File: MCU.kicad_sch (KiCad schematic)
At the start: 55 parts, among them IC1 BALFHB-WL-02D3, J2 Conn_Coaxial, J3 Led, Q2 S8050, Q3 S8050, SW1 SW_Push, U4 BGS12WN6E6327, U5 STM32WLE5CCUx, X1 NX2016SA-32MHZ, Y1 NX2012SA 32.768KHz

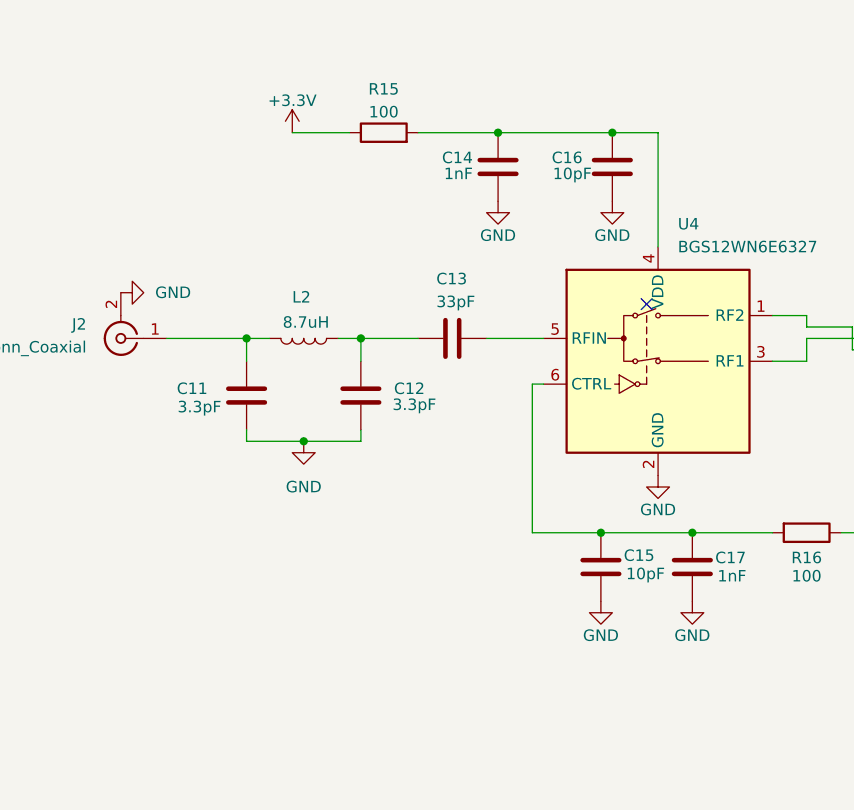
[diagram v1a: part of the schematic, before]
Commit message: removed polarity protection and fixed component placement
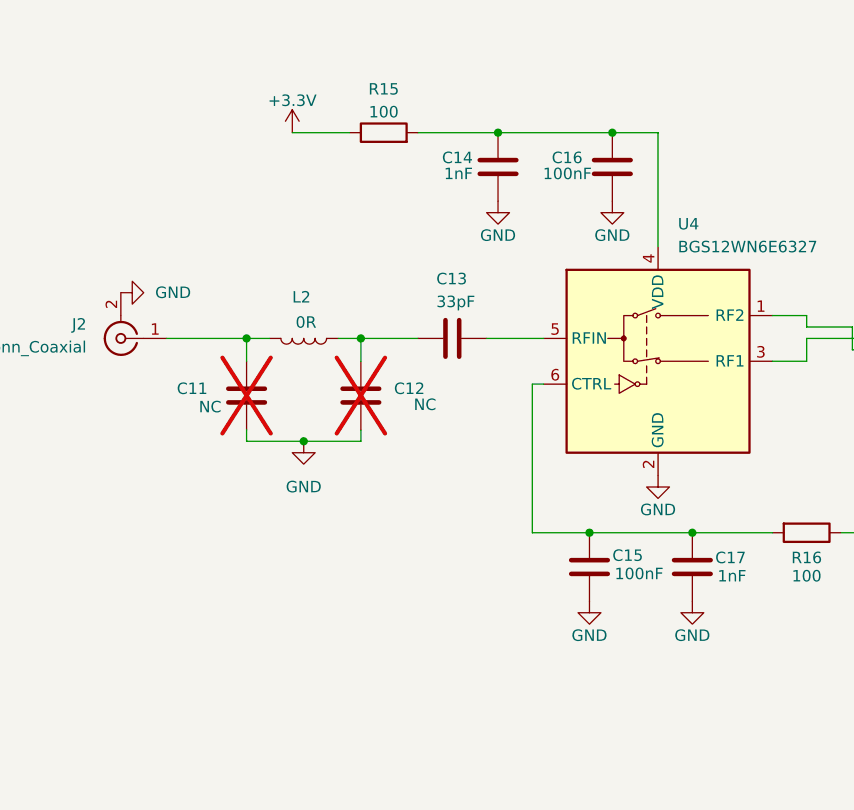
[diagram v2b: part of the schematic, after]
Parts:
- C11, C12: value 3.3pF -> NC; now not fitted; now left out of the parts list
- C15, C16: value 10pF -> 100nF
- L2: value 8.7uH -> 0R
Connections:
- no-connect marks 19 -> 18
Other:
- moved on the sheet: C15
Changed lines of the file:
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@@
 	)
 	(junction
+		(at 99.06 186.69)
+		(diameter 0)
+		(color 0 0 0 0)
+	)
+	(junction
 		(at 200.66 200.66)
 		(diameter 0)
@@
 	)
 	(junction
-		(at 100.33 186.69)
-		(diameter 0)
-		(color 0 0 0 0)
-	)
-	(junction
 		(at 273.05 40.64)
 		(diameter 0)
@@
 	)
 	(no_connect
-		(at 105.41 161.29)
-	)
-	(no_connect
 		(at 278.13 162.56)
 	)
@@
 	(wire
 		(pts
+			(xy 99.06 186.69) (xy 110.49 186.69)
+		)
+		(stroke
+			(width 0)
+			(type default)
+		)
+	)
+	(wire
+		(pts
 			(xy 119.38 167.64) (xy 123.19 167.64)
 		)
@@
 	(wire
 		(pts
+			(xy 99.06 186.69) (xy 92.71 186.69)
+		)
+		(stroke
+			(width 0)
+			(type default)
+		)
+	)
+	(wire
+		(pts
 			(xy 219.71 153.67) (xy 219.71 151.13)
 		)
@@
 	(wire
 		(pts
-			(xy 100.33 186.69) (xy 92.71 186.69)
-		)
-		(stroke
-			(width 0)
-			(type default)
-		)
-	)
-	(wire
-		(pts
 			(xy 144.78 165.1) (xy 147.32 165.1)
 		)
@@
 	(wire
 		(pts
-			(xy 110.49 186.69) (xy 100.33 186.69)
-		)
-		(stroke
-			(width 0)
-			(type default)
-		)
-	)
-	(wire
-		(pts
 			(xy 247.65 129.54) (xy 247.65 132.08)
 		)
@@
 	(symbol
 		(lib_id "Device:C")
-		(at 100.33 190.5 0)
+		(at 99.06 190.5 0)
 		(unit 1)
 		(exclude_from_sim no)
@@
 		(dnp no)
 		(property "Reference" "C15"
-			(at 102.87 189.23 0)
+			(at 101.6 189.23 0)
 			(effects
 				(font
@@
 			)
 		)
-		(property "Value" "10pF"
-			(at 103.124 191.262 0)
+		(property "Value" "100nF"
+			(at 101.854 191.262 0)
 			(effects
 				(font
@@
 		)
 		(property "Footprint" "Capacitor_SMD:C_0402_1005Metric_Pad0.74x0.62mm_HandSolder"
-			(at 101.2952 194.31 0)
+			(at 100.0252 194.31 0)
 			(effects
 				(font
@@
 		)
 		(property "Datasheet" "~"
-			(at 100.33 190.5 0)
+			(at 99.06 190.5 0)
 			(effects
 				(font
@@
 		)
 		(property "Description" ""
-			(at 100.33 190.5 0)
+			(at 99.06 190.5 0)
 			(effects
 				(font
@@
 		)
 		(property "MANUFACTURER" ""
-			(at 100.33 190.5 0)
+			(at 99.06 190.5 0)
 			(effects
 				(font
@@
 		)
 		(property "MAXIMUM_PACKAGE_HEIGHT" ""
-			(at 100.33 190.5 0)
+			(at 99.06 190.5 0)
 			(effects
 				(font
@@
 		)
 		(property "PARTREV" ""
-			(at 100.33 190.5 0)
+			(at 99.06 190.5 0)
 			(effects
 				(font
@@
 		)
 		(property "STANDARD" ""
-			(at 100.33 190.5 0)
+			(at 99.06 190.5 0)
 			(effects
 				(font
@@
 		(unit 1)
 		(exclude_from_sim no)
-		(in_bom yes)
+		(in_bom no)
 		(on_board yes)
-		(dnp no)
+		(dnp yes)
 		(property "Reference" "C12"
 			(at 80.772 170.688 0)
@@
 			)
 		)
-		(property "Value" "3.3pF"
+		(property "Value" "NC"
 			(at 82.042 172.466 0)
 			(effects
@@
 			)
 		)
-		(property "Value" "8.7uH"
+		(property "Value" "0R"
 			(at 67.564 163.322 90)
 			(effects
@@
 	(symbol
 		(lib_id "power:GND")
-		(at 100.33 194.31 0)
+		(at 99.06 194.31 0)
 		(unit 1)
 		(exclude_from_sim no)
@@
 		(dnp no)
 		(property "Reference" "#PWR016"
-			(at 100.33 200.66 0)
+			(at 99.06 200.66 0)
 			(effects
 				(font
@@
 		)
 		(property "Value" "GND"
-			(at 100.33 198.12 0)
+			(at 99.06 198.12 0)
 			(effects
 				(font
@@
 		)
 		(property "Footprint" ""
-			(at 100.33 194.31 0)
+			(at 99.06 194.31 0)
 			(effects
 				(font
@@
 		)
 		(property "Datasheet" ""
-			(at 100.33 194.31 0)
+			(at 99.06 194.31 0)
 			(effects
 				(font
@@
 		)
 		(property "Description" ""
-			(at 100.33 194.31 0)
+			(at 99.06 194.31 0)
 			(effects
 				(font
@@
 		(unit 1)
 		(exclude_from_sim no)
-		(in_bom yes)
+		(in_bom no)
 		(on_board yes)
-		(dnp no)
+		(dnp yes)
 		(property "Reference" "C11"
 			(at 56.642 170.688 0)
@@
 			)
 		)
-		(property "Value" "3.3pF"
+		(property "Value" "NC"
 			(at 58.166 172.72 0)
 			(effects
@@
 			)
 		)
-		(property "Value" "10pF"
+		(property "Value" "100nF"
 			(at 99.314 146.812 0)
 			(effects

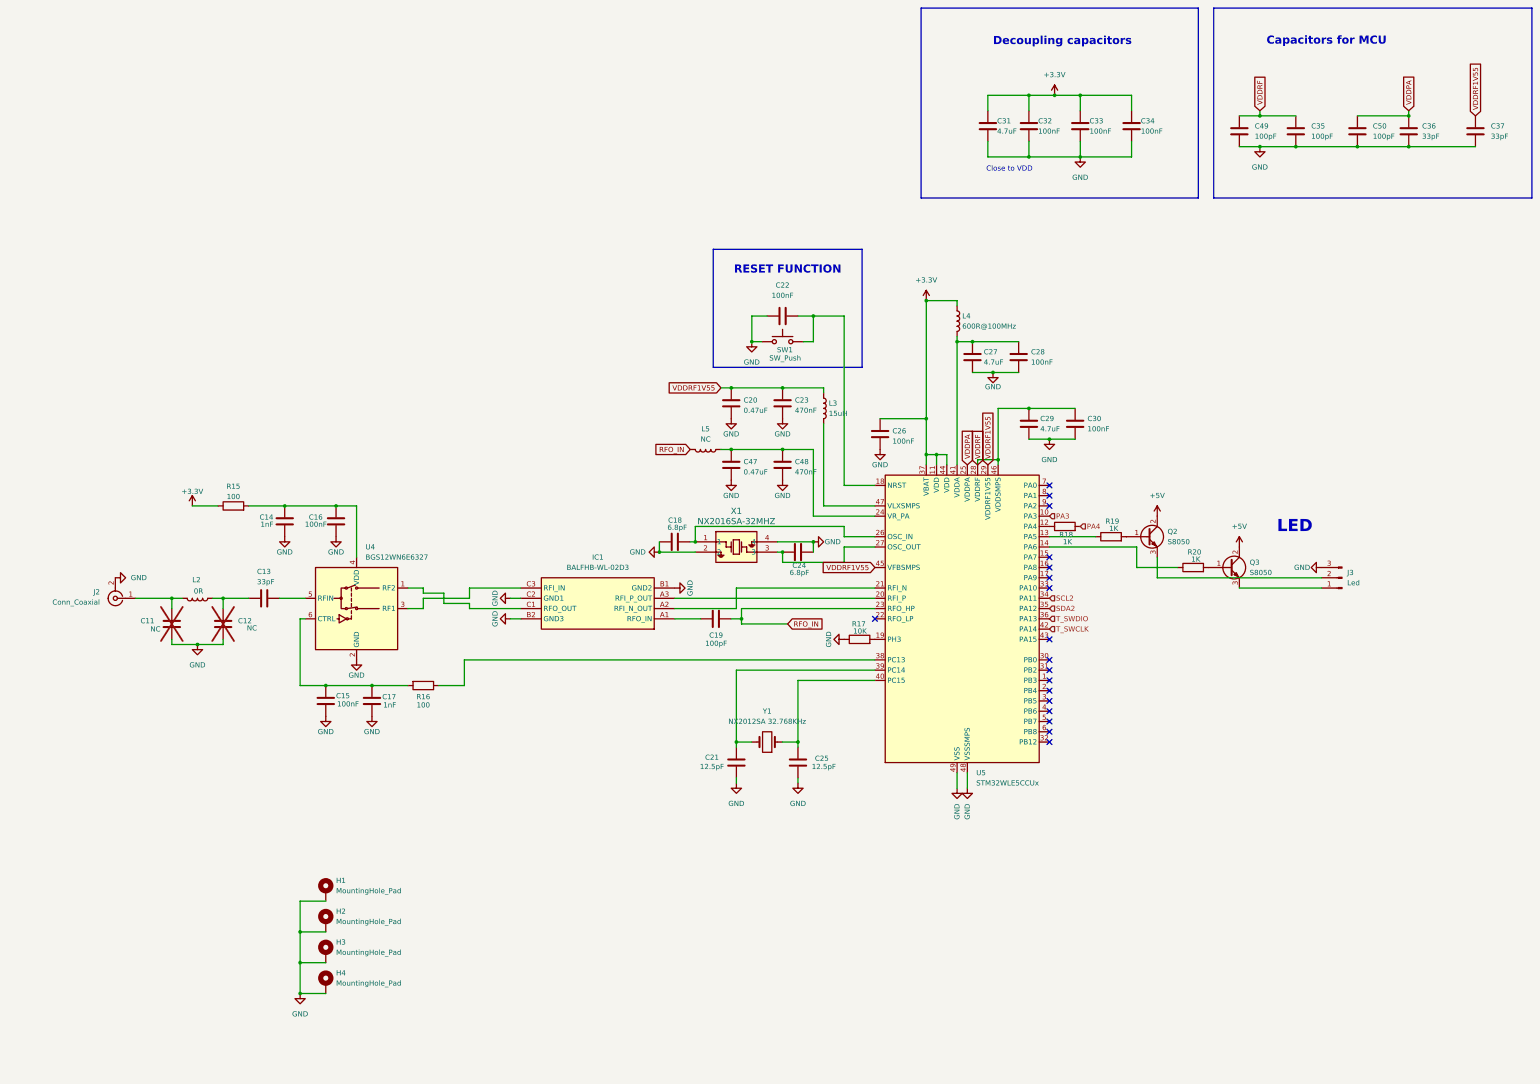
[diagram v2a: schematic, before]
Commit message: [Fix] Schematic and layout. - Replaced STM32WLE5x symbol for better visualization of the symbols - Added some missing connections - Modified some components' values - Changed the layout for STM32WL
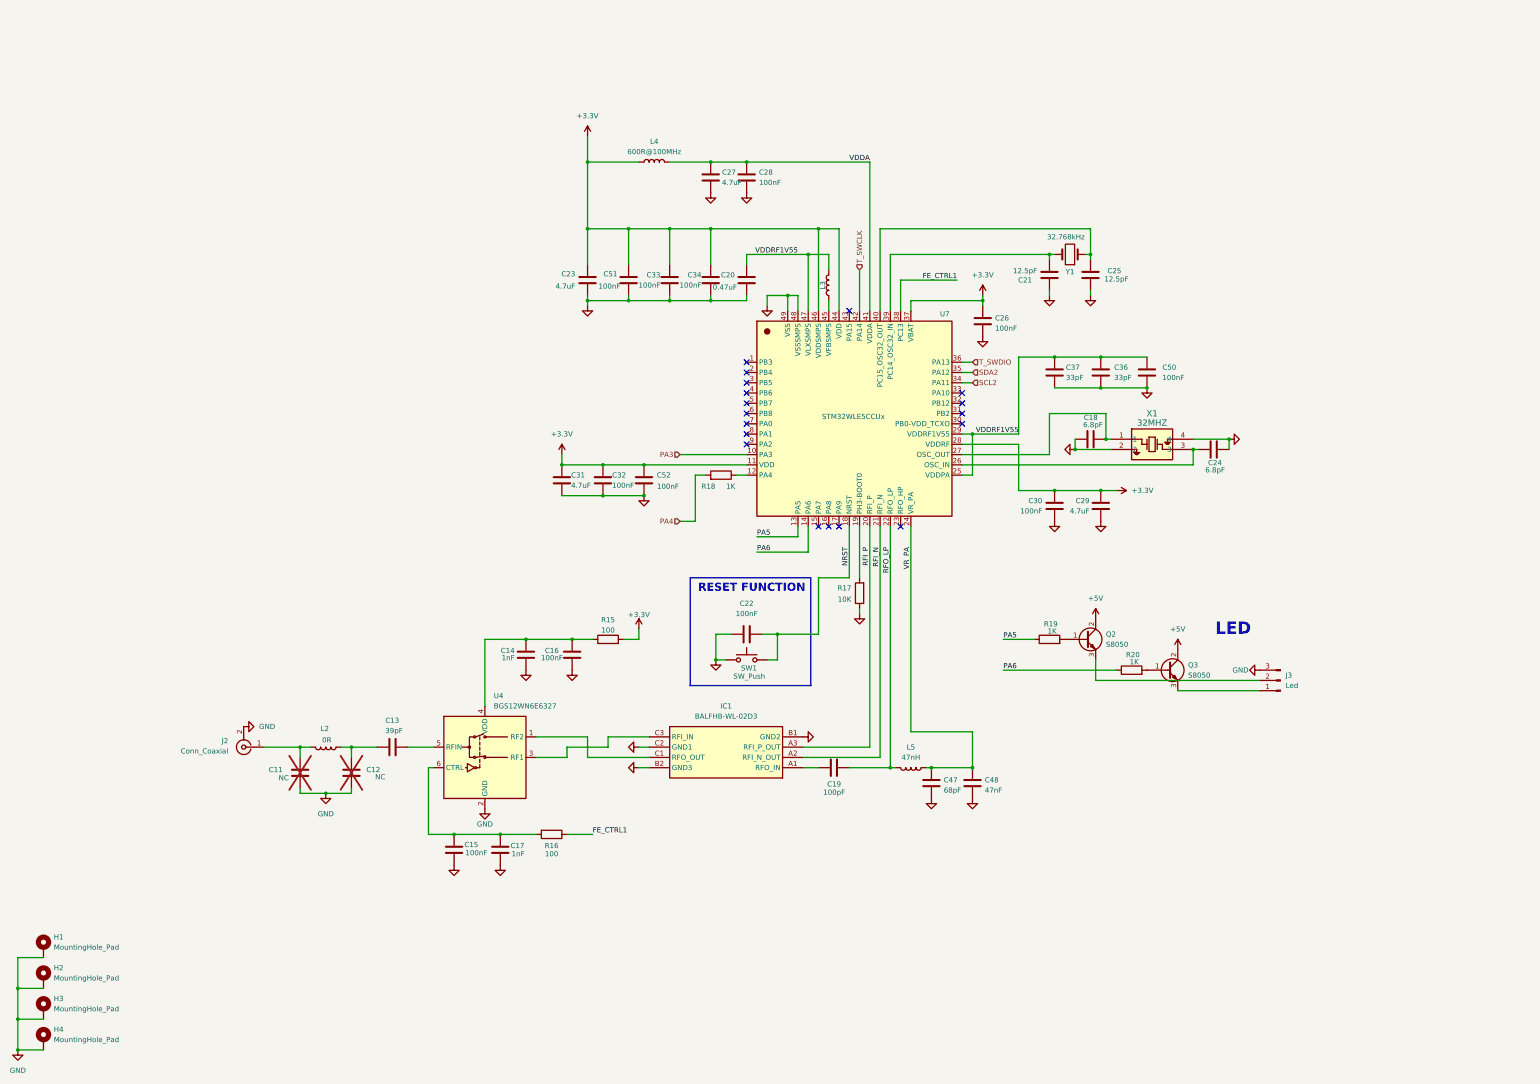
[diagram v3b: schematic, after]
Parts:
- removed C35, C49: 100pF, Capacitor_SMD:C_0402_1005Metric_Pad0.74x0.62mm_HandSolder, symbol Device:C
- removed U5: STM32WLE5CCUx, Package_DFN_QFN:QFN-48-1EP_7x7mm_P0.5mm_EP5.6x5.6mm, symbol MCU_ST_STM32WL:STM32WLE5CCUx
- added C51, C52: 100nF, Capacitor_SMD:C_0402_1005Metric, symbol Device:C
- added U7: STM32WLE5CCUx, Package_DFN_QFN:QFN-48-1EP_7x7mm_P0.5mm_EP5.6x5.6mm, symbol airlora:STM32WLE5CCUx
- C11, C12, C14, C15, C16, C17, C18, C19, C20, C21, C22, C24, C25, C26, C27, C28, C30, C32, C33, C34, C36, C37: footprint Capacitor_SMD:C_0402_1005Metric_Pad0.74x0.62mm_HandSolder -> Capacitor_SMD:C_0402_1005Metric
- C13: value 33pF -> 39pF; footprint Capacitor_SMD:C_0402_1005Metric_Pad0.74x0.62mm_HandSolder -> Capacitor_SMD:C_0402_1005Metric
- C23: value 470nF -> 4.7uF; footprint Capacitor_SMD:C_0402_1005Metric_Pad0.74x0.62mm_HandSolder -> Capacitor_SMD:C_0402_1005Metric
- C29, C31: footprint Capacitor_SMD:C_0402_1005Metric_Pad0.74x0.62mm_HandSolder -> Capacitor_SMD:C_0603_1608Metric
- C47: value 0.47uF -> 68pF; footprint Capacitor_SMD:C_0402_1005Metric_Pad0.74x0.62mm_HandSolder -> Capacitor_SMD:C_0402_1005Metric
- C48: value 470nF -> 47nF; footprint Capacitor_SMD:C_0402_1005Metric_Pad0.74x0.62mm_HandSolder -> Capacitor_SMD:C_0402_1005Metric
- C50: value 100pF -> 100nF; footprint Capacitor_SMD:C_0402_1005Metric_Pad0.74x0.62mm_HandSolder -> Capacitor_SMD:C_0402_1005Metric
- L2, L3, L4: footprint Inductor_SMD:L_0402_1005Metric_Pad0.77x0.64mm_HandSolder -> Inductor_SMD:L_0402_1005Metric
- L5: value NC -> 47nH; footprint Inductor_SMD:L_0402_1005Metric_Pad0.77x0.64mm_HandSolder -> Inductor_SMD:L_0402_1005Metric
- R15, R16, R17, R18, R19, R20: footprint Resistor_SMD:R_0402_1005Metric_Pad0.72x0.64mm_HandSolder -> Resistor_SMD:R_0402_1005Metric
- X1: value NX2016SA-32MHZ -> 32MHZ
- Y1: value NX2012SA 32.768KHz -> 32.768kHz
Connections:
- net VDDPA is gone; now on net VDDRF1V55: C36.1, C50.1
- net VDDRF is gone; now on net +3.3V: C29.1, C30.1
- net +3.3V: now also C23.1, R15.2, C51.2, C52.2, U7.11 (VDD), U7.28 (VDDRF), U7.37 (VBAT), U7.44 (VDD), U7.46 (VDDSMPS); no longer R15.1
- net GND: now also C21.2, C51.1, C52.1, U7.48 (VSSSMPS), U7.49 (VSS); no longer C21.1
- net PA3: now also U7.10 (PA3)
- net SCL2: now also U7.34 (PA11)
- net SDA2: now also U7.35 (PA12)
- net T_SWCLK: now also U7.42 (PA14)
- net T_SWDIO: now also U7.36 (PA13)
- net VDDRF1V55: now also L3.2, U7.25 (VDDPA), U7.29 (VDDRF1V55), U7.47 (VLXSMPS); no longer C23.1, L3.1
- net VDDA: now reaches C27.1, C28.1, L4.2
- net VDDA: now also U7.41 (VDDA)
- net VR_PA: now reaches C47.1, C48.1, L5.1
- net VR_PA: now also U7.24 (VR_PA)
- net PA6: now reaches R20.1
- net PA6: now also U7.14 (PA6)
- net RFI_N: now reaches IC1.A2 (RFI_N_OUT)
- net RFI_N: now also U7.21 (RFI_N)
- net RFI_P: now reaches IC1.A3 (RFI_P_OUT)
- net RFI_P: now also U7.20 (RFI_P)
- net at C18.2, X1.1: now also U7.27 (OSC_OUT)
- net FE_CTRL1: now reaches R16.1
- net FE_CTRL1: now also U7.38 (PC13)
- net at C25.2, Y1.1: now also U7.40 (PC15_OSC32_OUT)
- net at R18.1: now also U7.12 (PA4)
- net at C24.1, X1.3: now also U7.26 (OSC_IN)
- net at Y1.2: now also C21.1, U7.39 (PC14_OSC32_IN); no longer C21.2
- net PA5: now reaches R19.1
- net PA5: now also U7.13 (PA5)
- net NRST: now reaches C22.2, SW1.2
- net NRST: now also U7.18 (NRST)
- net at R17.2: now also U7.19 (PH3-BOOT0)
- net at C14.2, C16.2, U4.4 (VDD): now also R15.1; no longer R15.2
- net RFO_IN renamed RFO_LP
- net RFO_LP: now also U7.22 (RFO_LP)
- new net: L3.1, U7.45 (VFBSMPS)
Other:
- note removed: "Capacitors for MCU"
- note removed: "Close to VDD"
- note removed: "Decoupling capacitors"
- moved on the sheet: C11, C12, C13, C14, C15, C16, C17, C18, C19, C20, C21, C22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

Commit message: Update PCB layout
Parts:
- SW1: footprint Button_Switch_SMD:SW_Push_1P1T_NO_Vertical_Wuerth_434133025816 -> Button_Switch_THT:SW_Tactile_SPST_Angled_PTS645Vx39-2LFS
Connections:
- net at C24.1, X1.3: now also U7.27 (OSC_OUT); no longer U7.26 (OSC_IN)
- net at C18.2, X1.1: now also U7.26 (OSC_IN); no longer U7.27 (OSC_OUT)
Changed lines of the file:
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@@
 	)
 	(junction
+		(at 292.1 125.73)
+		(diameter 0)
+		(color 0 0 0 0)
+	)
+	(junction
 		(at 259.08 124.46)
 		(diameter 0)
@@
 	)
 	(junction
-		(at 160.02 175.26)
+		(at 314.96 128.27)
 		(diameter 0)
 		(color 0 0 0 0)
 	)
 	(junction
-		(at 290.83 138.43)
+		(at 160.02 175.26)
 		(diameter 0)
 		(color 0 0 0 0)
 	)
 	(junction
-		(at 322.58 125.73)
+		(at 290.83 138.43)
 		(diameter 0)
 		(color 0 0 0 0)
 	)
 	(junction
-		(at 292.1 125.73)
+		(at 322.58 125.73)
 		(diameter 0)
 		(color 0 0 0 0)
@@
 	)
 	(junction
-		(at 313.69 128.27)
-		(diameter 0)
-		(color 0 0 0 0)
-	)
-	(junction
 		(at 167.64 139.7)
 		(diameter 0)
@@
 	(wire
 		(pts
-			(xy 256.54 132.08) (xy 313.69 132.08)
+			(xy 256.54 132.08) (xy 292.1 132.08)
 		)
 		(stroke
@@
 	(wire
 		(pts
-			(xy 313.69 128.27) (xy 313.69 132.08)
-		)
-		(stroke
-			(width 0)
-			(type default)
-		)
-	)
-	(wire
-		(pts
 			(xy 92.71 201.93) (xy 92.71 204.47)
 		)
@@
 	(wire
 		(pts
-			(xy 292.1 119.38) (xy 278.13 119.38)
-		)
-		(stroke
-			(width 0)
-			(type default)
-		)
-	)
-	(wire
-		(pts
 			(xy 173.99 91.44) (xy 184.15 91.44)
 		)
@@
 	(wire
 		(pts
+			(xy 278.13 119.38) (xy 314.96 119.38)
+		)
+		(stroke
+			(width 0)
+			(type default)
+		)
+	)
+	(wire
+		(pts
 			(xy 194.31 73.66) (xy 220.98 73.66)
 		)
@@
 	(wire
 		(pts
+			(xy 314.96 119.38) (xy 314.96 128.27)
+		)
+		(stroke
+			(width 0)
+			(type default)
+		)
+	)
+	(wire
+		(pts
 			(xy 119.38 201.93) (xy 125.73 201.93)
 		)
@@
 	(wire
 		(pts
+			(xy 292.1 125.73) (xy 292.1 132.08)
+		)
+		(stroke
+			(width 0)
+			(type default)
+		)
+	)
+	(wire
+		(pts
 			(xy 195.58 180.34) (xy 198.12 180.34)
 		)
@@
 	(wire
 		(pts
-			(xy 292.1 125.73) (xy 292.1 119.38)
-		)
-		(stroke
-			(width 0)
-			(type default)
-		)
-	)
-	(wire
-		(pts
 			(xy 186.69 146.05) (xy 190.5 146.05)
 		)
@@
 			)
 		)
-		(property "Footprint" "Button_Switch_SMD:SW_Push_1P1T_NO_Vertical_Wuerth_434133025816"
+		(property "Footprint" "Button_Switch_THT:SW_Tactile_SPST_Angled_PTS645Vx39-2LFS"
 			(at 203.2 175.26 0)
 			(effects

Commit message: Update inductor
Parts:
- L3: footprint Inductor_SMD:L_0402_1005Metric -> Capacitor_SMD:C_0805_2012Metric
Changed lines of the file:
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@@
 			)
 		)
-		(property "Footprint" "Inductor_SMD:L_0402_1005Metric"
+		(property "Footprint" "Capacitor_SMD:C_0805_2012Metric"
 			(at 223.52 87.63 0)
 			(effects

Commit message: update problem
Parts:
- removed Q3: S8050, Package_TO_SOT_SMD:SOT-23, symbol Transistor_BJT:S8050
- added J12: UART_MAIN, Connector_JST:JST_XH_B4B-XH-A_1x04_P2.50mm_Vertical, symbol Connector:Screw_Terminal_01x04
- added Q2: S8050, Package_TO_SOT_SMD:SOT-23, symbol Transistor_BJT:S8050
- renumbered C15 to C14, C17 to C15, C14 to C16, C31 to C17, C16 to C18, C23 to C19, C32 to C20, C51 to C21, C52 to C22, C33 to C23, C27 to C24, C34 to C25, C28 to C26, C20 to C27, C22 to C28, C19 to C29, C47 to C30, C48 to C31, C26 to C32, C21 to C33, C37 to C34, C30 to C35, C25 to C36, C18 to C37, C36 to C38, C29 to C39, C50 to C40, C24 to C41, L4 to L3, L3 to L4, Q2 to Q1, R16 to R14, R18 to R16, R19 to R18, R20 to R19, U7 to U5
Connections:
- net +5V: now also Q1.3 (C), Q2.3 (C); no longer Q1.2 (C)
- net GND: now also J12.4 (Pin_4)
- net NRST: now also J12.3 (Pin_3)
- net at R19.2: now also Q2.1 (B)
- net RFO_HP: now reaches U5.23 (RFO_HP)
- net RFO_HP: now also C29.2, L5.2
- net UART1_TX: now reaches U5.4 (PB6)
- net UART1_TX: now also J12.2 (Pin_2)
- net UART1_RX: now reaches U5.5 (PB7)
- net UART1_RX: now also J12.1 (Pin_1)
- net at J3.2 (Pin_2): now also Q1.2 (E); no longer Q1.3 (E)
- net at J3.1 (Pin_1): now also Q2.2 (E)
- removed net RFO_LP: C29.2, L5.2, U5.22 (RFO_LP)
- no-connect marks 18 -> 16
